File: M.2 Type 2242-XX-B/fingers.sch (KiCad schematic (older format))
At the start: 7 parts, among them U7 M.2_NGFF_Socket2_KeyB_SSIC_Ad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

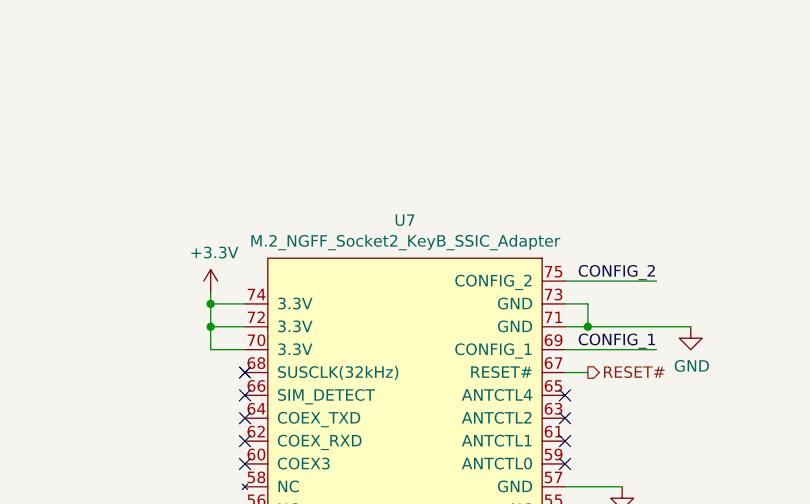
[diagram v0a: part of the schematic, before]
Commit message: Add proper footprint to solder jumpers
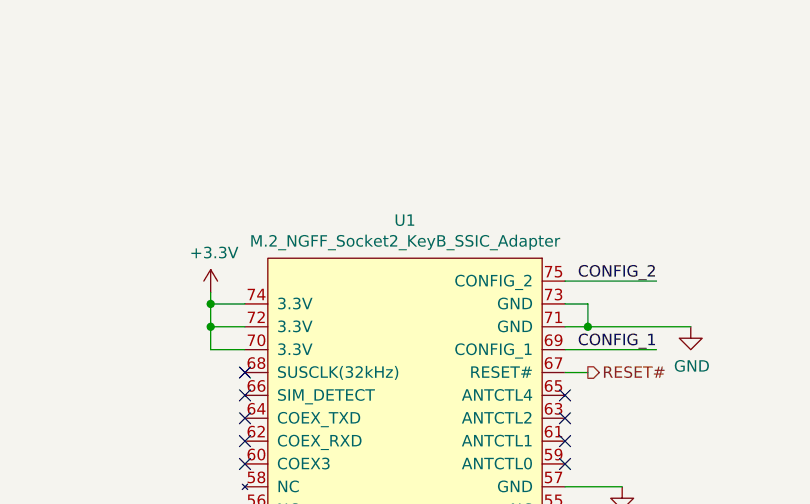
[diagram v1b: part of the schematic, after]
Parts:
- JP1, JP2, JP3: footprint (none) -> Jumper:SolderJumper-3_P1.3mm_Bridged12_RoundedPad1.0x1.5mm
- JP4: footprint (none) -> Jumper:SolderJumper-3_P1.3mm_Open_RoundedPad1.0x1.5mm
- renumbered U7 to U1
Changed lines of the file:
@@
 F 0 "JP1" V 7296 5968 50  0000 L CNN
 F 1 "CONFIG_0" V 7205 5968 50  0000 L CNN
-F 2 "" H 7250 5900 50  0001 C CNN
+F 2 "Jumper:SolderJumper-3_P1.3mm_Bridged12_RoundedPad1.0x1.5mm" H 7250 5900 50  0001 C CNN
 F 3 "~" H 7250 5900 50  0001 C CNN
 	1    7250 5900
@@
 F 0 "JP4" V 10546 5968 50  0000 L CNN
 F 1 "CONFIG_3" V 10455 5968 50  0000 L CNN
-F 2 "" H 10500 5900 50  0001 C CNN
+F 2 "Jumper:SolderJumper-3_P1.3mm_Open_RoundedPad1.0x1.5mm" H 10500 5900 50  0001 C CNN
 F 3 "~" H 10500 5900 50  0001 C CNN
 	1    10500 5900
@@
 F 0 "JP2" V 8396 5968 50  0000 L CNN
 F 1 "CONFIG_1" V 8305 5968 50  0000 L CNN
-F 2 "" H 8350 5900 50  0001 C CNN
+F 2 "Jumper:SolderJumper-3_P1.3mm_Bridged12_RoundedPad1.0x1.5mm" H 8350 5900 50  0001 C CNN
 F 3 "~" H 8350 5900 50  0001 C CNN
 	1    8350 5900
@@
 F 0 "JP3" V 9496 5968 50  0000 L CNN
 F 1 "CONFIG_2" V 9405 5968 50  0000 L CNN
-F 2 "" H 9450 5900 50  0001 C CNN
+F 2 "Jumper:SolderJumper-3_P1.3mm_Bridged12_RoundedPad1.0x1.5mm" H 9450 5900 50  0001 C CNN
 F 3 "~" H 9450 5900 50  0001 C CNN
 	1    9450 5900
@@
 P 3850 3850
 AR Path="/5DCE82AD" Ref="U?"  Part="1"
-AR Path="/5DCE3204/5DCE82AD" Ref="U7"  Part="1"
-F 0 "U7" H 3850 5965 50  0000 C CNN
+AR Path="/5DCE3204/5DCE82AD" Ref="U1"  Part="1"
+F 0 "U1" H 3850 5965 50  0000 C CNN
 F 1 "M.2_NGFF_Socket2_KeyB_SSIC_Adapter" H 3850 5874 50  0000 C CNN
 F 2 "M.2:M.2_Key_B_Fingers" H 5950 4150 50  0001 C CNN

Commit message: NOP Update
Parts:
- R22, R23: footprint (none) -> Resistor_SMD:R_0603_1608Metric
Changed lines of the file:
@@
 F 0 "R22" H 2520 5296 50  0000 L CNN
 F 1 "200K" H 2520 5205 50  0000 L CNN
-F 2 "" V 2380 5250 50  0001 C CNN
+F 2 "Resistor_SMD:R_0603_1608Metric" V 2380 5250 50  0001 C CNN
 F 3 "~" H 2450 5250 50  0001 C CNN
 	1    2450 5250
@@
 F 0 "R23" H 2520 5696 50  0000 L CNN
 F 1 "200K" H 2520 5605 50  0000 L CNN
-F 2 "" V 2380 5650 50  0001 C CNN
+F 2 "Resistor_SMD:R_0603_1608Metric" V 2380 5650 50  0001 C CNN
 F 3 "~" H 2450 5650 50  0001 C CNN
 	1    2450 5650

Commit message: Initial placement, I think we are going for the STM32F103 instead
The LQPF-100 is simply too big
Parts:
- R22, R23: footprint Resistor_SMD:R_0603_1608Metric -> Resistor_SMD:R_0402_1005Metric
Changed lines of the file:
@@
 F 0 "R22" H 2520 5296 50  0000 L CNN
 F 1 "200K" H 2520 5205 50  0000 L CNN
-F 2 "Resistor_SMD:R_0603_1608Metric" V 2380 5250 50  0001 C CNN
+F 2 "Resistor_SMD:R_0402_1005Metric" V 2380 5250 50  0001 C CNN
 F 3 "~" H 2450 5250 50  0001 C CNN
 	1    2450 5250
@@
 F 0 "R23" H 2520 5696 50  0000 L CNN
 F 1 "200K" H 2520 5605 50  0000 L CNN
-F 2 "Resistor_SMD:R_0603_1608Metric" V 2380 5650 50  0001 C CNN
+F 2 "Resistor_SMD:R_0402_1005Metric" V 2380 5650 50  0001 C CNN
 F 3 "~" H 2450 5650 50  0001 C CNN
 	1    2450 5650

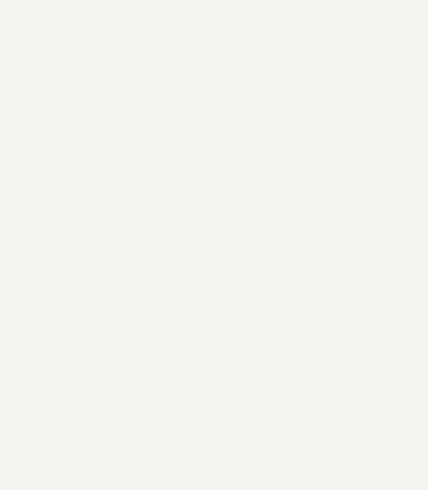
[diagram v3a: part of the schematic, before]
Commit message: Schematic updated to STM32F103
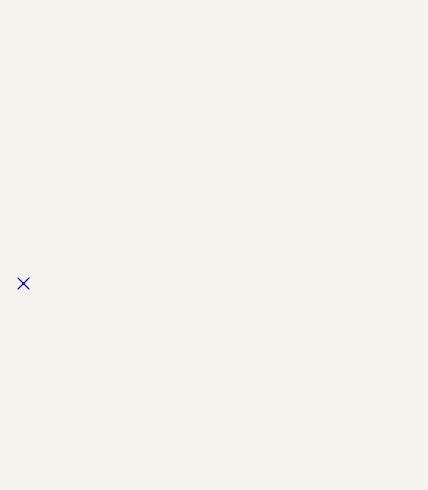
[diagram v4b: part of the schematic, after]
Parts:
- R22, R23: footprint Resistor_SMD:R_0402_1005Metric -> Resistor_SMD:R_0603_1608Metric
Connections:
- no-connect marks 25 -> 26
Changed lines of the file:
@@
 F 0 "R22" H 2520 5296 50  0000 L CNN
 F 1 "200K" H 2520 5205 50  0000 L CNN
-F 2 "Resistor_SMD:R_0402_1005Metric" V 2380 5250 50  0001 C CNN
+F 2 "Resistor_SMD:R_0603_1608Metric" V 2380 5250 50  0001 C CNN
 F 3 "~" H 2450 5250 50  0001 C CNN
 	1    2450 5250
@@
 F 0 "R23" H 2520 5696 50  0000 L CNN
 F 1 "200K" H 2520 5605 50  0000 L CNN
-F 2 "Resistor_SMD:R_0402_1005Metric" V 2380 5650 50  0001 C CNN
+F 2 "Resistor_SMD:R_0603_1608Metric" V 2380 5650 50  0001 C CNN
 F 3 "~" H 2450 5650 50  0001 C CNN
 	1    2450 5650
@@
 Wire Wire Line
 	4650 2400 4550 2400
+NoConn ~ -3150 5500
 $EndSCHEMATC

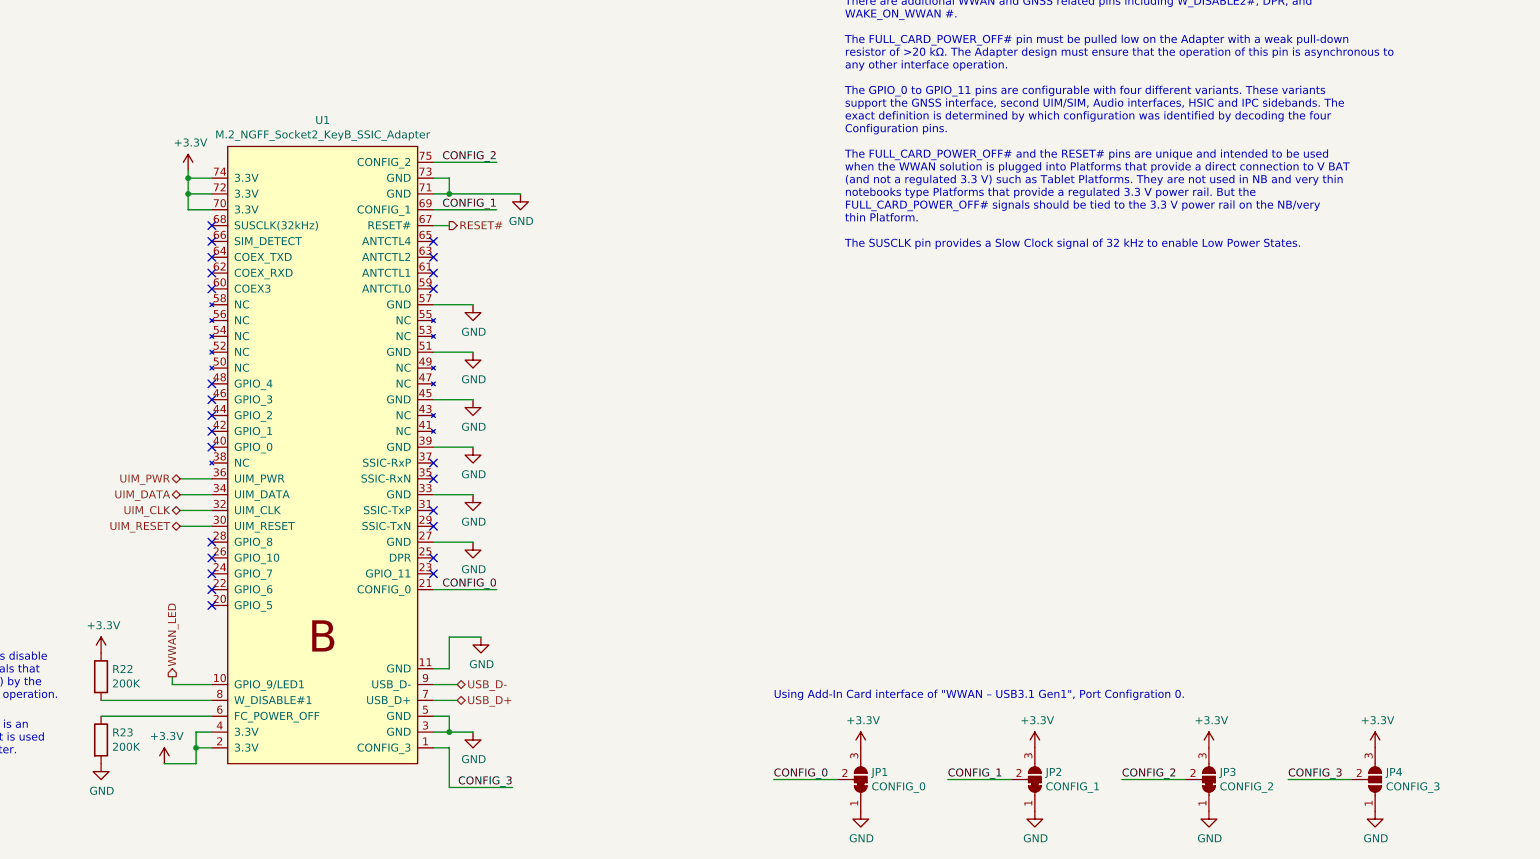
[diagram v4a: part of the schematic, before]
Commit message: Almost everything placed
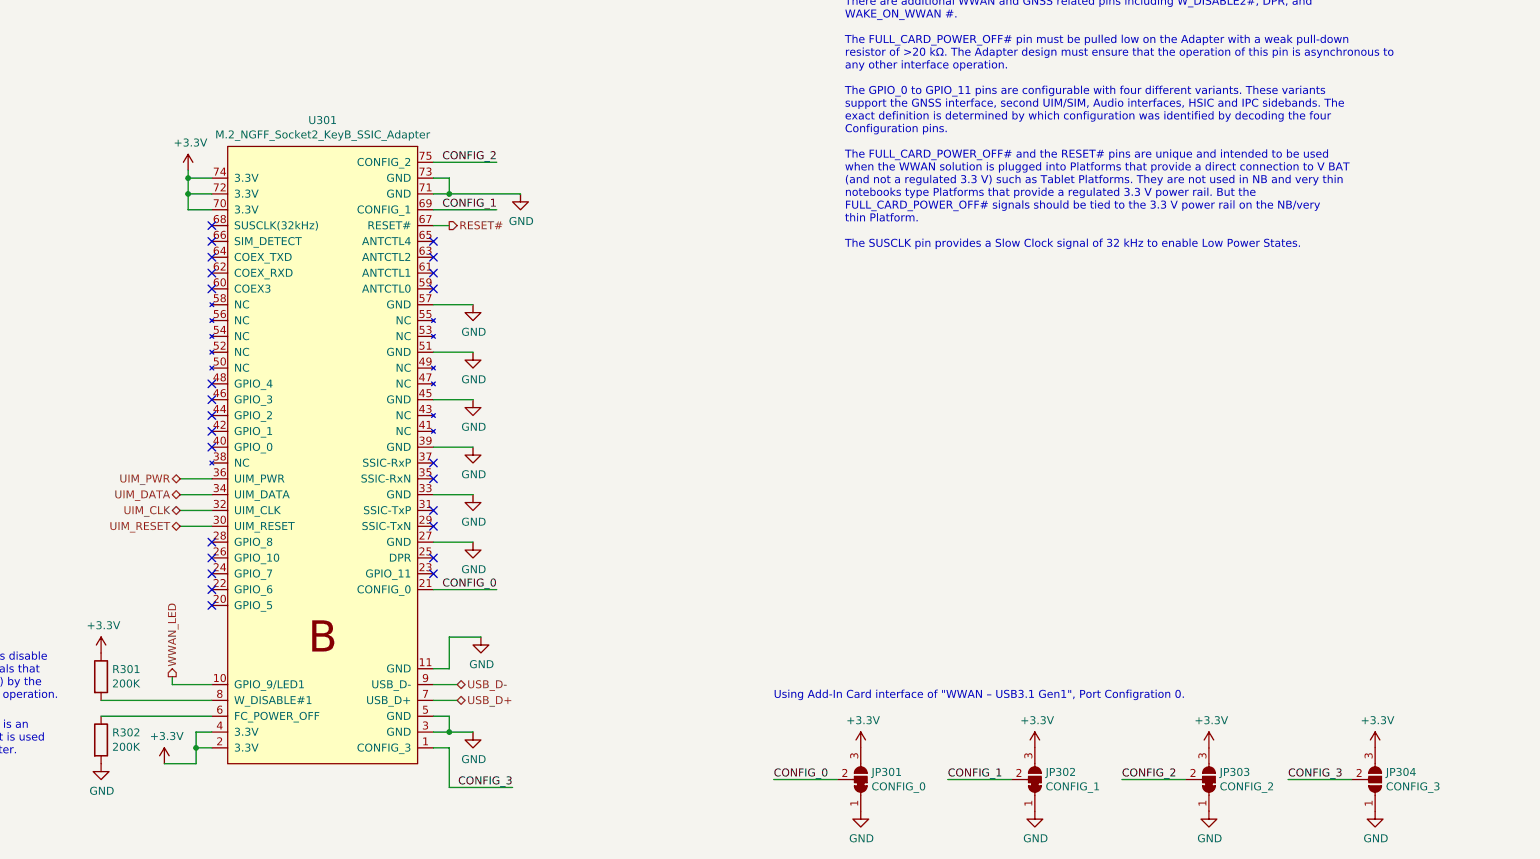
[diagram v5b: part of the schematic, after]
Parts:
- renumbered JP1 to JP301, JP2 to JP302, JP3 to JP303, JP4 to JP304, R22 to R301, R23 to R302, U1 to U301
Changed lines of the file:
@@
 P 3000 2050
 AR Path="/5DCE825A" Ref="#PWR?"  Part="1"
-AR Path="/5DCE3204/5DCE825A" Ref="#PWR0157"  Part="1"
-F 0 "#PWR0157" H 3000 1900 50  0001 C CNN
+AR Path="/5DCE3204/5DCE825A" Ref="#PWR0304"  Part="1"
+F 0 "#PWR0304" H 3000 1900 50  0001 C CNN
 F 1 "+3.3V" H 3015 2223 50  0000 C CNN
 F 2 "" H 3000 2050 50  0001 C CNN
@@
 P 2850 5800
 AR Path="/5DCE826D" Ref="#PWR?"  Part="1"
-AR Path="/5DCE3204/5DCE826D" Ref="#PWR0158"  Part="1"
-F 0 "#PWR0158" H 2850 5650 50  0001 C CNN
+AR Path="/5DCE3204/5DCE826D" Ref="#PWR0303"  Part="1"
+F 0 "#PWR0303" H 2850 5650 50  0001 C CNN
 F 1 "+3.3V" H 2865 5973 50  0000 C CNN
 F 2 "" H 2850 5800 50  0001 C CNN
@@
 P 4800 5600
 AR Path="/5DCE8274" Ref="#PWR?"  Part="1"
-AR Path="/5DCE3204/5DCE8274" Ref="#PWR0159"  Part="1"
-F 0 "#PWR0159" H 4800 5350 50  0001 C CNN
+AR Path="/5DCE3204/5DCE8274" Ref="#PWR0311"  Part="1"
+F 0 "#PWR0311" H 4800 5350 50  0001 C CNN
 F 1 "GND" H 4805 5427 50  0000 C CNN
 F 2 "" H 4800 5600 50  0001 C CNN
@@
 P 4800 4100
 AR Path="/5DCE827F" Ref="#PWR?"  Part="1"
-AR Path="/5DCE3204/5DCE827F" Ref="#PWR0160"  Part="1"
-F 0 "#PWR0160" H 4800 3850 50  0001 C CNN
+AR Path="/5DCE3204/5DCE827F" Ref="#PWR0309"  Part="1"
+F 0 "#PWR0309" H 4800 3850 50  0001 C CNN
 F 1 "GND" H 4805 3927 50  0000 C CNN
 F 2 "" H 4800 4100 50  0001 C CNN
@@
 P 4800 3800
 AR Path="/5DCE8286" Ref="#PWR?"  Part="1"
-AR Path="/5DCE3204/5DCE8286" Ref="#PWR0161"  Part="1"
-F 0 "#PWR0161" H 4800 3550 50  0001 C CNN
+AR Path="/5DCE3204/5DCE8286" Ref="#PWR0308"  Part="1"
+F 0 "#PWR0308" H 4800 3550 50  0001 C CNN
 F 1 "GND" H 4805 3627 50  0000 C CNN
 F 2 "" H 4800 3800 50  0001 C CNN
@@
 P 4800 3500
 AR Path="/5DCE828D" Ref="#PWR?"  Part="1"
-AR Path="/5DCE3204/5DCE828D" Ref="#PWR0162"  Part="1"
-F 0 "#PWR0162" H 4800 3250 50  0001 C CNN
+AR Path="/5DCE3204/5DCE828D" Ref="#PWR0307"  Part="1"
+F 0 "#PWR0307" H 4800 3250 50  0001 C CNN
 F 1 "GND" H 4805 3327 50  0000 C CNN
 F 2 "" H 4800 3500 50  0001 C CNN
@@
 P 4800 3200
 AR Path="/5DCE8294" Ref="#PWR?"  Part="1"
-AR Path="/5DCE3204/5DCE8294" Ref="#PWR0163"  Part="1"
-F 0 "#PWR0163" H 4800 2950 50  0001 C CNN
+AR Path="/5DCE3204/5DCE8294" Ref="#PWR0306"  Part="1"
+F 0 "#PWR0306" H 4800 2950 50  0001 C CNN
 F 1 "GND" H 4805 3027 50  0000 C CNN
 F 2 "" H 4800 3200 50  0001 C CNN
@@
 P 4800 2900
 AR Path="/5DCE829B" Ref="#PWR?"  Part="1"
-AR Path="/5DCE3204/5DCE829B" Ref="#PWR0164"  Part="1"
-F 0 "#PWR0164" H 4800 2650 50  0001 C CNN
+AR Path="/5DCE3204/5DCE829B" Ref="#PWR0305"  Part="1"
+F 0 "#PWR0305" H 4800 2650 50  0001 C CNN
 F 1 "GND" H 4805 2727 50  0000 C CNN
 F 2 "" H 4800 2900 50  0001 C CNN
@@
 P 5100 2200
 AR Path="/5DCE82A2" Ref="#PWR?"  Part="1"
-AR Path="/5DCE3204/5DCE82A2" Ref="#PWR0165"  Part="1"
-F 0 "#PWR0165" H 5100 1950 50  0001 C CNN
+AR Path="/5DCE3204/5DCE82A2" Ref="#PWR0313"  Part="1"
+F 0 "#PWR0313" H 5100 1950 50  0001 C CNN
 F 1 "GND" H 5105 2027 50  0000 C CNN
 F 2 "" H 5100 2200 50  0001 C CNN
@@
 P 4850 5000
 AR Path="/5DCEA3E4" Ref="#PWR?"  Part="1"
-AR Path="/5DCE3204/5DCEA3E4" Ref="#PWR0166"  Part="1"
-F 0 "#PWR0166" H 4850 4750 50  0001 C CNN
+AR Path="/5DCE3204/5DCEA3E4" Ref="#PWR0312"  Part="1"
+F 0 "#PWR0312" H 4850 4750 50  0001 C CNN
 F 1 "GND" H 4855 4827 50  0000 C CNN
 F 2 "" H 4850 5000 50  0001 C CNN
@@
 P 4800 4400
 AR Path="/5DCEC5D6" Ref="#PWR?"  Part="1"
-AR Path="/5DCE3204/5DCEC5D6" Ref="#PWR0167"  Part="1"
-F 0 "#PWR0167" H 4800 4150 50  0001 C CNN
+AR Path="/5DCE3204/5DCEC5D6" Ref="#PWR0310"  Part="1"
+F 0 "#PWR0310" H 4800 4150 50  0001 C CNN
 F 1 "GND" H 4805 4227 50  0000 C CNN
 F 2 "" H 4800 4400 50  0001 C CNN
@@
 NoConn ~ 4550 2500
 $Comp
-L Device:R R22
+L Device:R R301
 U 1 1 5E0D4B51
 P 2450 5250
-F 0 "R22" H 2520 5296 50  0000 L CNN
+F 0 "R301" H 2520 5296 50  0000 L CNN
 F 1 "200K" H 2520 5205 50  0000 L CNN
 F 2 "Resistor_SMD:R_0603_1608Metric" V 2380 5250 50  0001 C CNN
@@
 P 2450 5100
 AR Path="/5E0D5CA6" Ref="#PWR?"  Part="1"
-AR Path="/5DCE3204/5E0D5CA6" Ref="#PWR0168"  Part="1"
-F 0 "#PWR0168" H 2450 4950 50  0001 C CNN
+AR Path="/5DCE3204/5E0D5CA6" Ref="#PWR0301"  Part="1"
+F 0 "#PWR0301" H 2450 4950 50  0001 C CNN
 F 1 "+3.3V" H 2465 5273 50  0000 C CNN
 F 2 "" H 2450 5100 50  0001 C CNN
@@
 	2900 5300 2900 5250
 $Comp
-L Device:R R23
+L Device:R R302
 U 1 1 5E0D8EEA
 P 2450 5650
-F 0 "R23" H 2520 5696 50  0000 L CNN
+F 0 "R302" H 2520 5696 50  0000 L CNN
 F 1 "200K" H 2520 5605 50  0000 L CNN
 F 2 "Resistor_SMD:R_0603_1608Metric" V 2380 5650 50  0001 C CNN
@@
 P 2450 5800
 AR Path="/5E0DA1E8" Ref="#PWR?"  Part="1"
-AR Path="/5DCE3204/5E0DA1E8" Ref="#PWR0169"  Part="1"
-F 0 "#PWR0169" H 2450 5550 50  0001 C CNN
+AR Path="/5DCE3204/5E0DA1E8" Ref="#PWR0302"  Part="1"
+F 0 "#PWR0302" H 2450 5550 50  0001 C CNN
 F 1 "GND" H 2455 5627 50  0000 C CNN
 F 2 "" H 2450 5800 50  0001 C CNN
@@
 W_DISABLE#1 The wireless disable\nsignals are active low signals that\nwhen asserted (driven low) by the\nsystem must disable radio operation.
 $Comp
-L power:GND #PWR0170
+L power:GND #PWR0315
 U 1 1 5E0E1DA8
 P 7250 6100
-F 0 "#PWR0170" H 7250 5850 50  0001 C CNN
+F 0 "#PWR0315" H 7250 5850 50  0001 C CNN
 F 1 "GND" H 7255 5927 50  0000 C CNN
 F 2 "" H 7250 6100 50  0001 C CNN
@@
 $EndComp
 $Comp
-L power:+3.3V #PWR0171
+L power:+3.3V #PWR0314
 U 1 1 5E0E23B3
 P 7250 5700
-F 0 "#PWR0171" H 7250 5550 50  0001 C CNN
+F 0 "#PWR0314" H 7250 5550 50  0001 C CNN
 F 1 "+3.3V" H 7265 5873 50  0000 C CNN
 F 2 "" H 7250 5700 50  0001 C CNN
@@
 $EndComp
 $Comp
-L Jumper:SolderJumper_3_Bridged12 JP1
+L Jumper:SolderJumper_3_Bridged12 JP301
 U 1 1 5E0DD0F3
 P 7250 5900
-F 0 "JP1" V 7296 5968 50  0000 L CNN
+F 0 "JP301" V 7296 5968 50  0000 L CNN
 F 1 "CONFIG_0" V 7205 5968 50  0000 L CNN
 F 2 "Jumper:SolderJumper-3_P1.3mm_Bridged12_RoundedPad1.0x1.5mm" H 7250 5900 50  0001 C CNN
@@
 $EndComp
 $Comp
-L Jumper:SolderJumper_3_Open JP4
+L Jumper:SolderJumper_3_Open JP304
 U 1 1 5E0E3B56
 P 10500 5900
-F 0 "JP4" V 10546 5968 50  0000 L CNN
+F 0 "JP304" V 10546 5968 50  0000 L CNN
 F 1 "CONFIG_3" V 10455 5968 50  0000 L CNN
 F 2 "Jumper:SolderJumper-3_P1.3mm_Open_RoundedPad1.0x1.5mm" H 10500 5900 50  0001 C CNN
@@
 $EndComp
 $Comp
-L power:GND #PWR0172
+L power:GND #PWR0317
 U 1 1 5E0E6DC0
 P 8350 6100
-F 0 "#PWR0172" H 8350 5850 50  0001 C CNN
+F 0 "#PWR0317" H 8350 5850 50  0001 C CNN
 F 1 "GND" H 8355 5927 50  0000 C CNN
 F 2 "" H 8350 6100 50  0001 C CNN
@@
 $EndComp
 $Comp
-L power:+3.3V #PWR0173
+L power:+3.3V #PWR0316
 U 1 1 5E0E6DCA
 P 8350 5700
-F 0 "#PWR0173" H 8350 5550 50  0001 C CNN
+F 0 "#PWR0316" H 8350 5550 50  0001 C CNN
 F 1 "+3.3V" H 8365 5873 50  0000 C CNN
 F 2 "" H 8350 5700 50  0001 C CNN
@@
 $EndComp
 $Comp
-L Jumper:SolderJumper_3_Bridged12 JP2
+L Jumper:SolderJumper_3_Bridged12 JP302
 U 1 1 5E0E6DD4
 P 8350 5900
-F 0 "JP2" V 8396 5968 50  0000 L CNN
+F 0 "JP302" V 8396 5968 50  0000 L CNN
 F 1 "CONFIG_1" V 8305 5968 50  0000 L CNN
 F 2 "Jumper:SolderJumper-3_P1.3mm_Bridged12_RoundedPad1.0x1.5mm" H 8350 5900 50  0001 C CNN
@@
 	7800 5900 8200 5900
 $Comp
-L power:GND #PWR0174
+L power:GND #PWR0319
 U 1 1 5E0EB4BE
 P 9450 6100
-F 0 "#PWR0174" H 9450 5850 50  0001 C CNN
+F 0 "#PWR0319" H 9450 5850 50  0001 C CNN
 F 1 "GND" H 9455 5927 50  0000 C CNN
 F 2 "" H 9450 6100 50  0001 C CNN
@@
 $EndComp
 $Comp
-L power:+3.3V #PWR0175
+L power:+3.3V #PWR0318
 U 1 1 5E0EB4C8
 P 9450 5700
-F 0 "#PWR0175" H 9450 5550 50  0001 C CNN
+F 0 "#PWR0318" H 9450 5550 50  0001 C CNN
 F 1 "+3.3V" H 9465 5873 50  0000 C CNN
 F 2 "" H 9450 5700 50  0001 C CNN
@@
 $EndComp
 $Comp
-L Jumper:SolderJumper_3_Bridged12 JP3
+L Jumper:SolderJumper_3_Bridged12 JP303
 U 1 1 5E0EB4D2
 P 9450 5900
-F 0 "JP3" V 9496 5968 50  0000 L CNN
+F 0 "JP303" V 9496 5968 50  0000 L CNN
 F 1 "CONFIG_2" V 9405 5968 50  0000 L CNN
 F 2 "Jumper:SolderJumper-3_P1.3mm_Bridged12_RoundedPad1.0x1.5mm" H 9450 5900 50  0001 C CNN
@@
 	4550 2300 4950 2300
 $Comp
-L power:GND #PWR0176
+L power:GND #PWR0321
 U 1 1 5E0FBF8A
 P 10500 6100
-F 0 "#PWR0176" H 10500 5850 50  0001 C CNN
+F 0 "#PWR0321" H 10500 5850 50  0001 C CNN
 F 1 "GND" H 10505 5927 50  0000 C CNN
 F 2 "" H 10500 6100 50  0001 C CNN
@@
 $EndComp
 $Comp
-L power:+3.3V #PWR0177
+L power:+3.3V #PWR0320
 U 1 1 5E0FCD03
 P 10500 5700
-F 0 "#PWR0177" H 10500 5550 50  0001 C CNN
+F 0 "#PWR0320" H 10500 5550 50  0001 C CNN
 F 1 "+3.3V" H 10515 5873 50  0000 C CNN
 F 2 "" H 10500 5700 50  0001 C CNN
@@
 P 3850 3850
 AR Path="/5DCE82AD" Ref="U?"  Part="1"
-AR Path="/5DCE3204/5DCE82AD" Ref="U1"  Part="1"
-F 0 "U1" H 3850 5965 50  0000 C CNN
+AR Path="/5DCE3204/5DCE82AD" Ref="U301"  Part="1"
+F 0 "U301" H 3850 5965 50  0000 C CNN
 F 1 "M.2_NGFF_Socket2_KeyB_SSIC_Adapter" H 3850 5874 50  0000 C CNN
 F 2 "M.2:M.2_Key_B_Fingers" H 5950 4150 50  0001 C CNN
